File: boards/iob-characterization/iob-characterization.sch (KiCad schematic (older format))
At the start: 86 parts, among them J1 BARREL, J2 GREENPAK_DEVKIT_HDR, P1 TESTCLIP, P10 SMA_TE_5-1814832-1, P11 SMT_TESTPOINT, P12 SMT_TESTPOINT, P13 SMT_TESTPOINT, P14 SMT_TESTPOINT, P15 TESTCLIP, P16 TESTCLIP, P17 SMA_TE_5-1814832-1, P18 SMA_TE_5-1814832-1, P19 SMT_TESTPOINT, P2 SMT_TESTPOINT, P20 JUMPER, P21 JUMPER, P22 TESTCLIP, P23 TESTCLIP, P24 JUMPER, P25 JUMPER, P26 JUMPER, P27 TESTCLIP, P28 TESTCLIP, P29 SMA_TE_5-1814832-1, P3 SMT_TESTPOINT, P4 SMT_TESTPOINT, P5 SMT_TESTPOINT, P6 SMT_TESTPOINT, P7 SMT_TESTPOINT, P8 SMA_TE_5-1814832-1, P9 SMA_TE_5-1814832-1, Q1 BSS214N_H6327, Q2 SSM6N58NU, Q3 BSS214N_H6327, Q4 SSM6N58NU, U1 ADCMP607_LFCSP, U2 TLV1117-33-DFN, U3 74LVC1G66_SOT353, U4 74LVC1G66_SOT353, U5 SIP32408, U6 SIP32408, U7 74LVC1T45, U8 74AVCH2T45

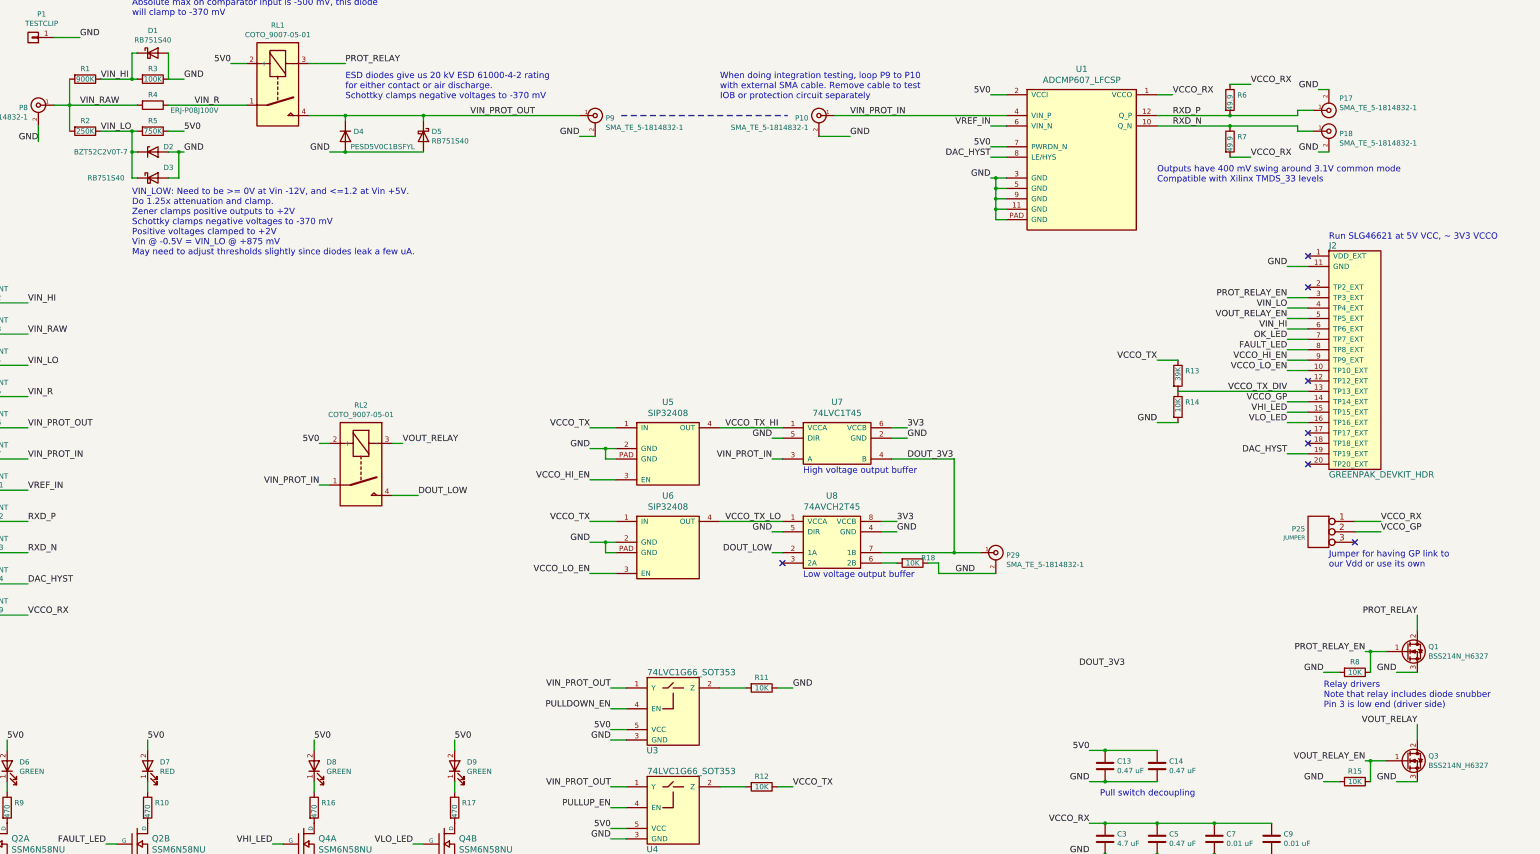
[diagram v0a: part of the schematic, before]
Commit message: Updated IOB characterization board with full footprints for all components. No real layout yet.
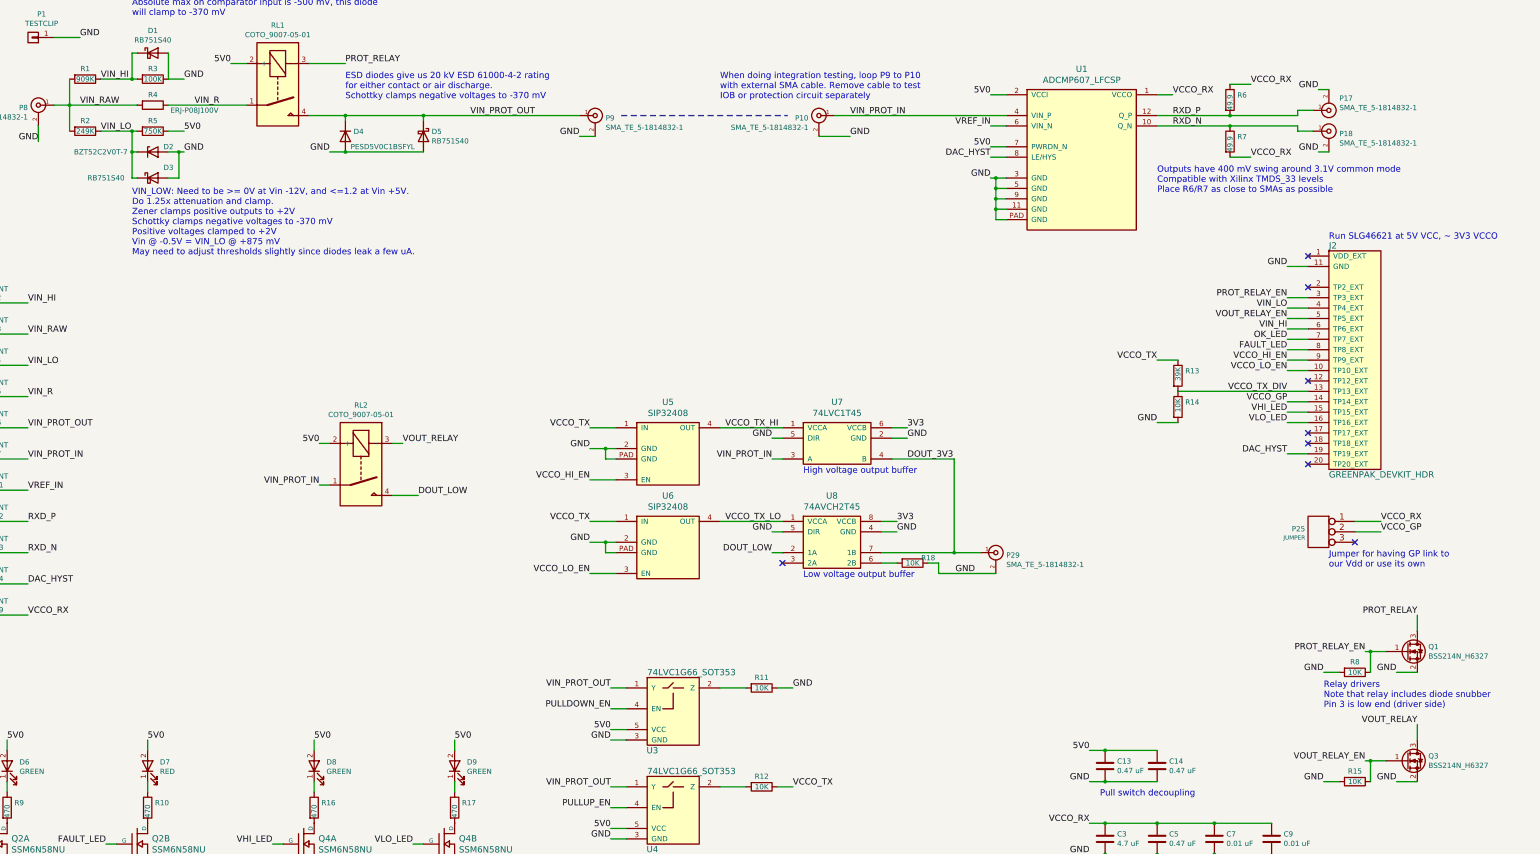
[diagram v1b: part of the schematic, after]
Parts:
- removed Q1, Q3: BSS214N_H6327, symbol Q_NMOS_GDS
- removed RL1, RL2: COTO_9007-05-01, symbol RM50-xx21
- added Q1, Q3: BSS214N_H6327, azonenberg_pcb:SOT23_3, symbol Q_NMOS_GSD
- added RL1, RL2: COTO_9007-05-01, azonenberg_pcb:RELAY_COTO_9007, symbol RELAY_COTO_9007
- C1, C11, C12, C2, C3, C4: footprint (none) -> azonenberg_pcb:EIA_0603_CAP_NOSILK
- C10, C13, C14, C5, C6, C7, C8, C9: footprint (none) -> azonenberg_pcb:EIA_0402_CAP_NOSILK
- D1, D3, D5: footprint (none) -> azonenberg_pcb:SOD523F
- D2: footprint (none) -> azonenberg_pcb:SOD523
- D4: footprint (none) -> azonenberg_pcb:SOD962_2
- D6, D7, D8, D9: footprint (none) -> azonenberg_pcb:EIA_0603_LED
- J1: footprint (none) -> azonenberg_pcb:CONN_CUI_PJ-058BH_HIPWR_BARREL_NOSLOT
- J2: footprint (none) -> azonenberg_pcb:CONN_HEADER_2.54MM_2x10_RA_FEMALE
- P1, P15, P16, P22, P23, P27, P28: footprint (none) -> azonenberg_pcb:TESTPOINT_SMT_KEYSTONE_5016
- P10, P17, P18, P29, P8, P9: footprint (none) -> azonenberg_pcb:CONN_SMA_PTH
- P11, P12, P13, P14, P19, P2, P3, P4, P5, P6, P7: footprint (none) -> azonenberg_pcb:TESTPOINT_SMT_0.5MM
- P20, P21, P24, P25, P26: footprint (none) -> azonenberg_pcb:CONN_HEADER_2.54MM_1x3
- Q2, Q4: footprint (none) -> azonenberg_pcb:DFN_6_0.65MM_2x2MM_GDS
- R1: value 900K -> 909K; footprint (none) -> azonenberg_pcb:EIA_0402_RES_NOSILK
- R10, R11, R12, R13, R14, R15, R16, R17, R18, R3, R5, R6, R7, R8, R9: footprint (none) -> azonenberg_pcb:EIA_0402_RES_NOSILK
- R2: value 250K -> 249K; footprint (none) -> azonenberg_pcb:EIA_0402_RES_NOSILK
- R4: footprint (none) -> azonenberg_pcb:EIA_1206_CAP_NOSILK
- U1: footprint (none) -> azonenberg_pcb:QFN_12_0.5MM_3x3MM
- U2: footprint (none) -> azonenberg_pcb:DFN_8_0.8MM_4x4MM
- U3, U4: footprint (none) -> azonenberg_pcb:SOT353_1
- U5, U6: footprint (none) -> azonenberg_pcb:DFN_4_0.5MM_1.6x1.2MM
- U7: footprint (none) -> azonenberg_pcb:SOT363
- U8: footprint (none) -> azonenberg_pcb:DFN_8_0.5MM_2x1MM
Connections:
- net 5V0: now also RL1.2 (+), RL2.2 (+)
- net DOUT_LOW: now also RL2.4
- net GND: now also Q1.2 (S), Q3.2 (S)
- net PROT_RELAY: now also Q1.3 (D), RL1.3 (-)
- net PROT_RELAY_EN: now also Q1.1 (G)
- net VIN_PROT_IN: now also RL2.1
- net VIN_PROT_OUT: now also RL1.4
- net VIN_R: now also RL1.1
- net VOUT_RELAY: now also Q3.3 (D), RL2.3 (-)
- net VOUT_RELAY_EN: now also Q3.1 (G)
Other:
- note added: "Outputs have 400 mV swing around 3.1V common mode\nCompatible with Xilinx TMDS_33 levels\nPlace R6/R7 as close to SMAs as possible"
- note removed: "Outputs have 400 mV swing around 3.1V common mode\nCompatible with Xilinx TMDS_33 levels"

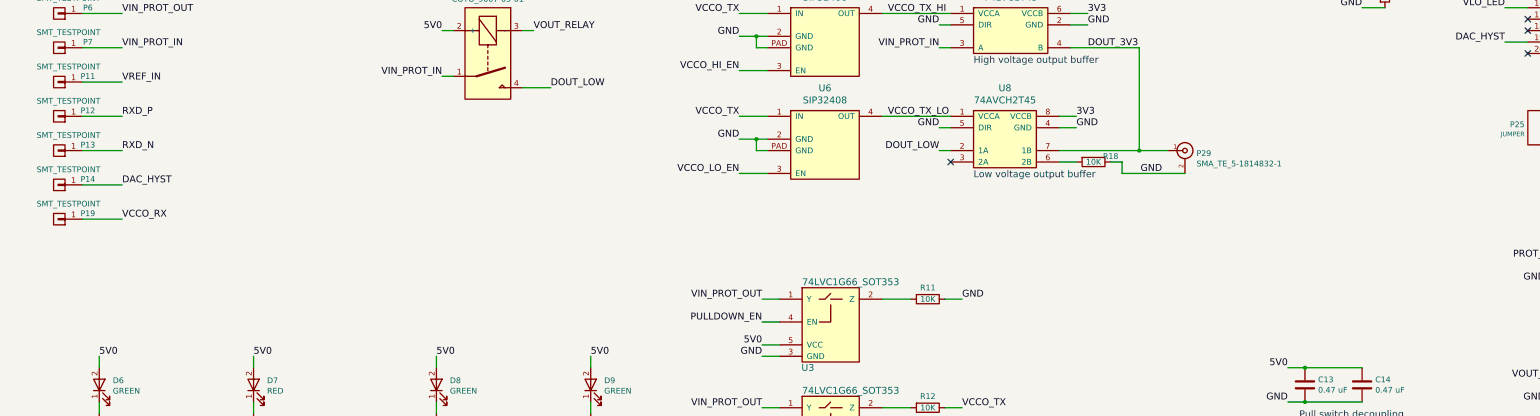
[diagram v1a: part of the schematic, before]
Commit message: Finished initial I/O buffer characterization board layout
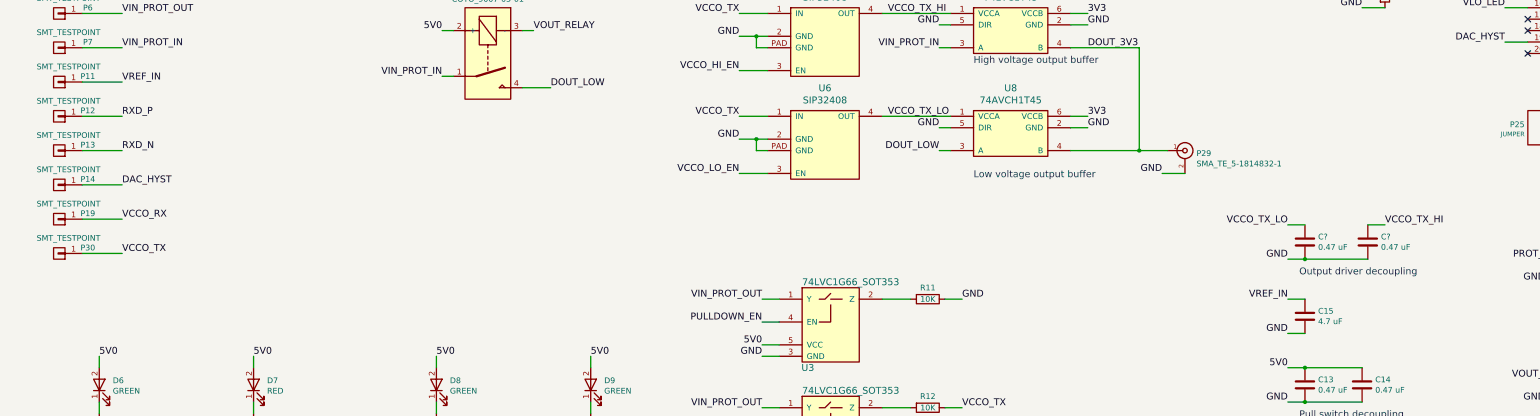
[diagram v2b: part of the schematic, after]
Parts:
- removed R18: 10K, azonenberg_pcb:EIA_0402_RES_NOSILK, symbol R
- removed U8: 74AVCH2T45, azonenberg_pcb:DFN_8_0.5MM_2x1MM, symbol 74AVCH2T45
- added C15: 4.7 uF, azonenberg_pcb:EIA_0603_CAP_NOSILK, symbol C
- added C? (x2): 0.47 uF, azonenberg_pcb:EIA_0402_CAP_NOSILK, symbol C
- added P30: SMT_TESTPOINT, azonenberg_pcb:TESTPOINT_SMT_0.5MM, symbol CONN_01X01
- added U8: 74AVCH1T45, azonenberg_pcb:SOT363, symbol 74LVC1T45
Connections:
- net 3V3: now also U8.6 (VCCB)
- net DOUT_3V3: now also U8.4 (B)
- net DOUT_LOW: now also U8.3 (A)
- net GND: now also C15.2, C?.2, C?.2, U8.2 (GND), U8.5 (DIR)
- net VCCO_TX: now also P30.1 (P1)
- net VCCO_TX_HI: now also C?.1
- net VCCO_TX_LO: now also C?.1, U8.1 (VCCA)
- net VREF_IN: now also C15.1
- no-connect marks 8 -> 7
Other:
- note added: "Output driver decoupling"
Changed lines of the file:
@@
 Sheet 1 1
 Title "STARSHIPRAIDER I/O Buffer Characterization Board"
-Date "2016-12-28"
+Date "2016-12-29"
 Rev "0.1"
 Comp "Andrew Zonenberg"
@@
 Text Label 4300 5600 2    60   ~ 0
 VIN_PROT_IN
-$Comp
-L 74AVCH2T45 U8
-U 1 1 58663593
-P 8950 6400
-F 0 "U8" H 9225 7097 60  0000 C CNN
-F 1 "74AVCH2T45" H 9225 6991 60  0000 C CNN
-F 2 "azonenberg_pcb:DFN_8_0.5MM_2x1MM" H 8950 6400 60  0001 C CNN
-F 3 "" H 8950 6400 60  0001 C CNN
-	1    8950 6400
-	1    0    0    -1
-$EndComp
 Text Notes 8950 6500 0    60   ~ 0
 Low voltage output buffer
@@
 Text Label 9950 5150 0    60   ~ 0
 GND
-Text Label 9850 6050 0    60   ~ 0
+Text Label 9950 6050 0    60   ~ 0
 GND
 Text Label 9950 5050 0    60   ~ 0
 3V3
-Text Label 9850 5950 0    60   ~ 0
+Text Label 9950 5950 0    60   ~ 0
 3V3
 Text Notes 8950 5500 0    60   ~ 0
@@
 	8150 5950 8750 5950
 Wire Wire Line
-	9850 6350 9700 6350
-Wire Wire Line
 	8150 5050 8750 5050
 Wire Wire Line
@@
 	9950 5150 9800 5150
 Wire Wire Line
-	9850 6050 9700 6050
+	9950 6050 9800 6050
 Wire Wire Line
 	9950 5050 9800 5050
 Wire Wire Line
-	9850 5950 9700 5950
+	9950 5950 9800 5950
 Wire Wire Line
 	8650 5350 8750 5350
@@
 Wire Wire Line
 	9800 5350 10400 5350
-Wire Wire Line
-	9700 6250 10650 6250
 Wire Wire Line
 	10400 5350 10400 6250
 Connection ~ 10400 6250
-Wire Wire Line
-	10250 6450 10800 6450
 Wire Wire Line
 	6900 5050 7150 5050
@@
 Wire Wire Line
 	13600 5000 13800 5000
-NoConn ~ 8750 6350
-$Comp
-L R R18
-U 1 1 5865188B
-P 10000 6350
-F 0 "R18" V 9950 6500 50  0000 C CNN
-F 1 "10K" V 10000 6350 50  0000 C CNN
-F 2 "azonenberg_pcb:EIA_0402_RES_NOSILK" V 9930 6350 50  0001 C CNN
-F 3 "" H 10000 6350 50  0000 C CNN
-	1    10000 6350
-	0    1    1    0
-$EndComp
-Wire Wire Line
-	10150 6350 10250 6350
-Wire Wire Line
-	10250 6350 10250 6450
 $Comp
 L RELAY_COTO_9007 RL1
@@
 	1    0    0    -1
 $EndComp
+$Comp
+L C C15
+U 1 1 5867E68B
+P 11850 7700
+F 0 "C15" H 11965 7746 50  0000 L CNN
+F 1 "4.7 uF" H 11965 7655 50  0000 L CNN
+F 2 "azonenberg_pcb:EIA_0603_CAP_NOSILK" H 11888 7550 50  0001 C CNN
+F 3 "" H 11850 7700 50  0000 C CNN
+	1    11850 7700
+	1    0    0    -1
+$EndComp
+Text Label 11700 7550 2    60   ~ 0
+VREF_IN
+Wire Wire Line
+	11700 7550 11850 7550
+Text Label 11700 7850 2    60   ~ 0
+GND
+Wire Wire Line
+	11700 7850 11850 7850
+$Comp
+L 74LVC1T45 U8
+U 1 1 5865F420
+P 8950 6300
+F 0 "U8" H 9275 6897 60  0000 C CNN
+F 1 "74AVCH1T45" H 9275 6791 60  0000 C CNN
+F 2 "azonenberg_pcb:SOT363" H 8950 6300 60  0001 C CNN
+F 3 "" H 8950 6300 60  0001 C CNN
+	1    8950 6300
+	1    0    0    -1
+$EndComp
+Wire Wire Line
+	10800 6450 10600 6450
+Wire Wire Line
+	9800 6250 10650 6250
+Text Label 1500 7150 0    60   ~ 0
+VCCO_TX
+$Comp
+L CONN_01X01 P30
+U 1 1 586630A4
+P 950 7150
+F 0 "P30" H 700 7100 50  0000 C CNN
+F 1 "SMT_TESTPOINT" H 869 7016 50  0000 C CNN
+F 2 "azonenberg_pcb:TESTPOINT_SMT_0.5MM" H 950 7150 50  0001 C CNN
+F 3 "" H 950 7150 50  0000 C CNN
+	1    950  7150
+	-1   0    0    1
+$EndComp
+Wire Wire Line
+	1500 7150 1150 7150
+$Comp
+L C C?
+U 1 1 58664F34
+P 11850 7050
+F 0 "C?" H 11965 7096 50  0000 L CNN
+F 1 "0.47 uF" H 11965 7005 50  0000 L CNN
+F 2 "azonenberg_pcb:EIA_0402_CAP_NOSILK" H 11888 6900 50  0001 C CNN
+F 3 "" H 11850 7050 50  0000 C CNN
+	1    11850 7050
+	1    0    0    -1
+$EndComp
+Text Notes 11800 7350 0    60   ~ 0
+Output driver decoupling
+Text Label 11700 6900 2    60   ~ 0
+VCCO_TX_LO
+Text Label 11700 7200 2    60   ~ 0
+GND
+Wire Wire Line
+	11700 7200 12400 7200
+$Comp
+L C C?
+U 1 1 58665CB4
+P 12400 7050
+F 0 "C?" H 12515 7096 50  0000 L CNN
+F 1 "0.47 uF" H 12515 7005 50  0000 L CNN
+F 2 "azonenberg_pcb:EIA_0402_CAP_NOSILK" H 12438 6900 50  0001 C CNN
+F 3 "" H 12400 7050 50  0000 C CNN
+	1    12400 7050
+	1    0    0    -1
+$EndComp
+Text Label 12550 6900 0    60   ~ 0
+VCCO_TX_HI
+Wire Wire Line
+	12550 6900 12400 6900
+Connection ~ 11850 7200
+Wire Wire Line
+	11850 6900 11700 6900
 $EndSCHEMATC

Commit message: Pushing current version of characterization board
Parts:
- gave numbers to parts that had none: 2
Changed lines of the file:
@@
 	1500 7150 1150 7150
 $Comp
-L C C?
+L C C16
 U 1 1 58664F34
 P 11850 7050
-F 0 "C?" H 11965 7096 50  0000 L CNN
+F 0 "C16" H 11965 7096 50  0000 L CNN
 F 1 "0.47 uF" H 11965 7005 50  0000 L CNN
 F 2 "azonenberg_pcb:EIA_0402_CAP_NOSILK" H 11888 6900 50  0001 C CNN
@@
 	11700 7200 12400 7200
 $Comp
-L C C?
+L C C17
 U 1 1 58665CB4
 P 12400 7050
-F 0 "C?" H 12515 7096 50  0000 L CNN
+F 0 "C17" H 12515 7096 50  0000 L CNN
 F 1 "0.47 uF" H 12515 7005 50  0000 L CNN
 F 2 "azonenberg_pcb:EIA_0402_CAP_NOSILK" H 12438 6900 50  0001 C CNN
